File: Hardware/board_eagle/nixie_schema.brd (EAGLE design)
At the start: 150 x 170 mm, 110 parts, among them P1 100k, P2 10k, Q1 BC856B, Q3 BC856B, Q4 BCX70H, Q5 NTF5P03, U2 MC7940N

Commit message: Hopefully fixed compined tube footprint for good
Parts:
- moved N6 239.8 mm to (-5.00, -244.0), turned to 0 degrees
- moved N5 205.9 mm to (-5.00, -218.0), turned to 0 degrees
- moved N4 168.7 mm to (-5.00, -192.0), turned to 0 degrees
- moved N3 135.0 mm to (-5.00, -166.0), turned to 0 degrees
- moved N2 98.9 mm to (-5.00, -140.0), turned to 0 degrees
- moved N1 66.8 mm to (-5.00, -114.0), turned to 0 degrees
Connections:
- net N$10: now also N1.A(A); no longer N1.A(NC)
- net N$19: now also N2.A(A); no longer N2.A(NC)
- net N$2: now also N1.6(CAT); no longer N1.6(G)
- net N$21: now also N3.A(A); no longer N3.A(NC)
- net N$23: now also N2.6(CAT); no longer N2.6(G)
- net N$24: now also N1.9(DP); no longer N1.9(D)
- net N$25: now also N1.1(F); no longer N1.1(GRID)
- net N$26: now also N1.2(E); no longer N1.2(C)
- net N$27: now also N1.3(D); no longer N1.3(DP)
- net N$28: now also N1.4(CAT); no longer N1.4(B)
- net N$29: now also N1.5(NC); no longer N1.5(A)
- net N$31: now also N2.7(GRID); no longer N2.7(F)
- net N$32: now also N2.8(C); no longer N2.8(E)
- net N$33: now also N2.9(DP); no longer N2.9(D)
- net N$34: now also N2.0(B); no longer N2.0(CAT)
- net N$36: now also N3.6(CAT)
- net N$37: now also N3.7(GRID)
- net N$38: now also N2.5(NC); no longer N2.5(A)
- net N$39: now also N2.4(CAT); no longer N2.4(B)
- net N$40: now also N2.3(D); no longer N2.3(DP)
- net N$41: now also N2.2(E); no longer N2.2(C)
- net N$42: now also N2.1(F); no longer N2.1(GRID)
- net N$43: now also N3.8(C)
- net N$44: now also N3.9(DP)
- net N$45: now also N6.A(A); no longer N6.A(NC)
- net N$46: now also N3.0(B)
- net N$48: now also N4.6(CAT)
- net N$49: now also N3.5(NC)
- net N$50: now also N3.4(CAT)
- net N$51: now also N3.3(D)
- net N$52: now also N3.2(E)
- net N$53: now also N3.1(F)
- net N$54: now also N4.7(GRID)
- net N$55: now also N4.8(C)
- net N$56: now also N4.9(DP)
- net N$57: now also N4.0(B)
- net N$59: now also N4.5(NC)
- net N$6: now also N1.7(GRID); no longer N1.7(F)
- net N$60: now also N4.4(CAT)
- net N$61: now also N4.3(D)
- net N$62: now also N4.2(E)
- net N$63: now also N4.1(F)
- net N$64: now also N5.6(CAT)
- net N$65: now also N5.7(GRID)
- net N$66: now also N5.8(C)
- net N$67: now also N5.9(DP)
- net N$68: now also N5.0(B)
- net N$69: now also N5.5(NC)
- net N$7: now also N1.8(C); no longer N1.8(E)
- net N$70: now also N5.4(CAT)
- net N$71: now also N5.3(D)
- net N$72: now also N5.2(E)
- net N$73: now also N5.1(F)
- net N$76: now also N6.6(CAT)
- net N$77: now also N6.7(GRID)
- net N$78: now also N6.8(C)
- net N$79: now also N6.9(DP)
- net N$80: now also N6.5(NC)
- net N$81: now also N6.4(CAT)
- net N$82: now also N6.3(D)
- net N$83: now also N6.2(E)
- net N$84: now also N6.1(F)
- net N$86: now also N6.0(B)
- net N$88: now also N4.A(A); no longer N4.A(NC)
- net N$94: now also N1.0(B); no longer N1.0(CAT)
- net N$98: now also N5.A(A); no longer N5.A(NC)

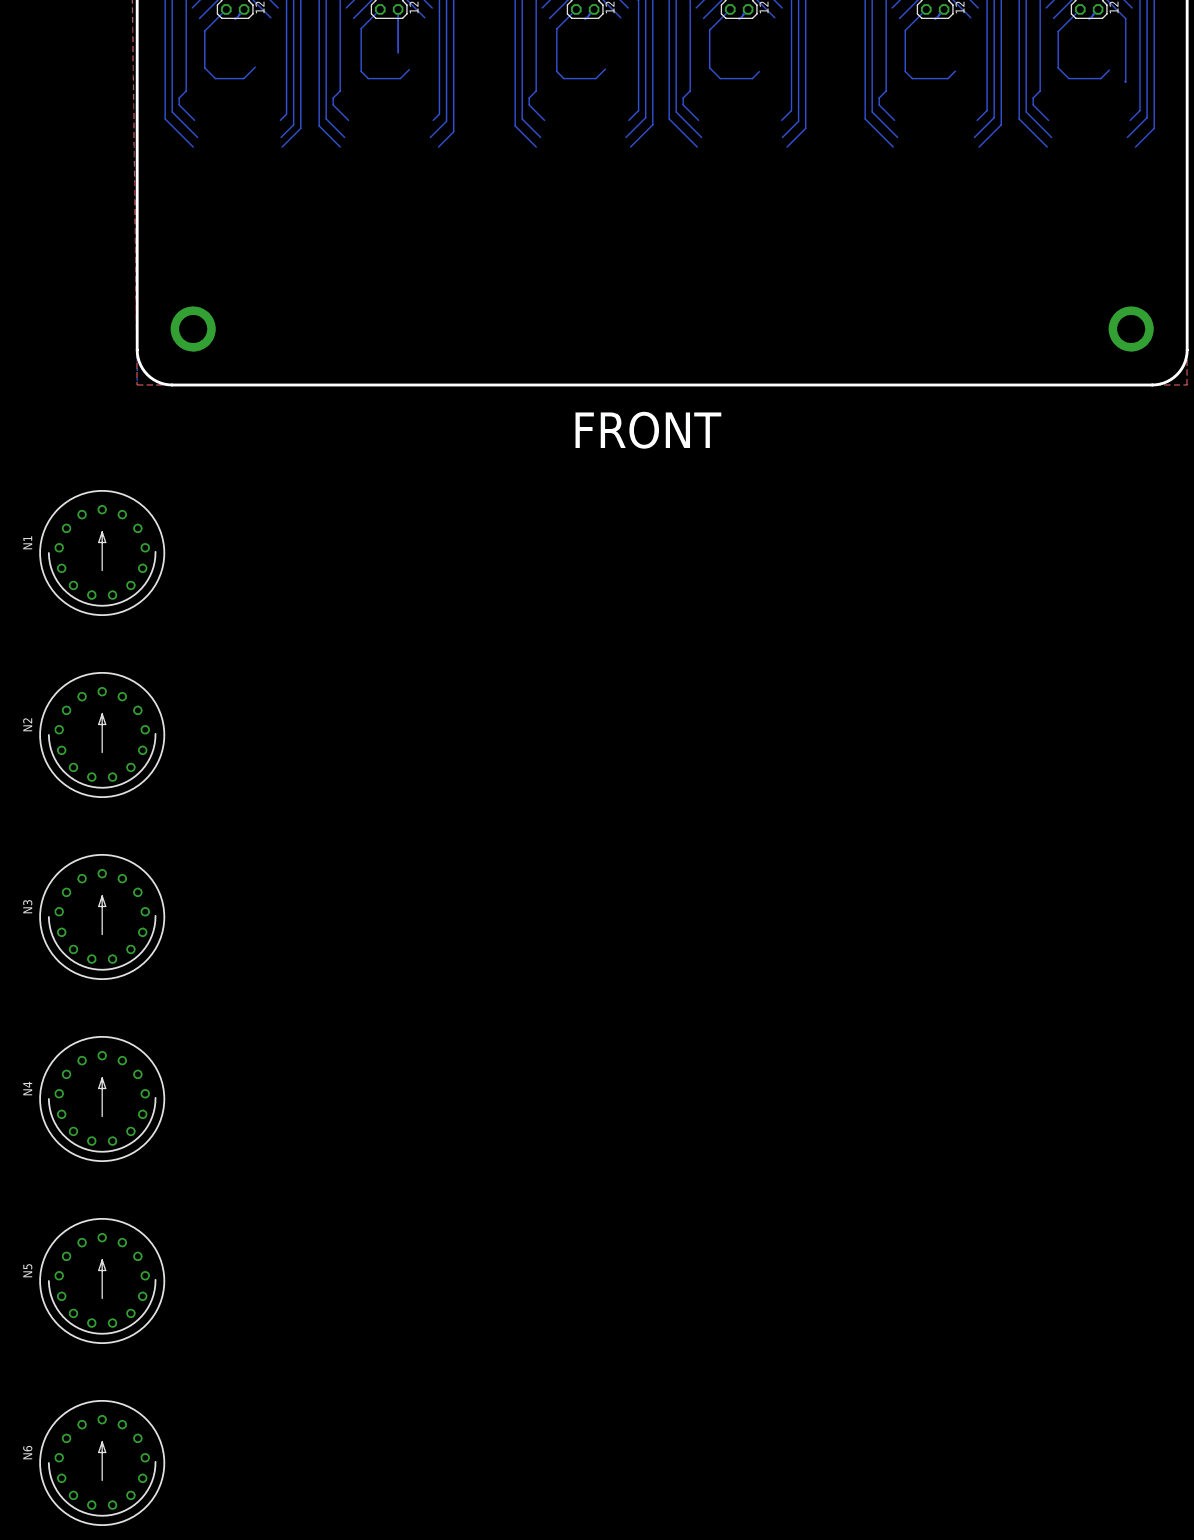
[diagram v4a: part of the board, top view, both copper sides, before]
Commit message: Added stuff for 1V5 rail for VFD cathodes
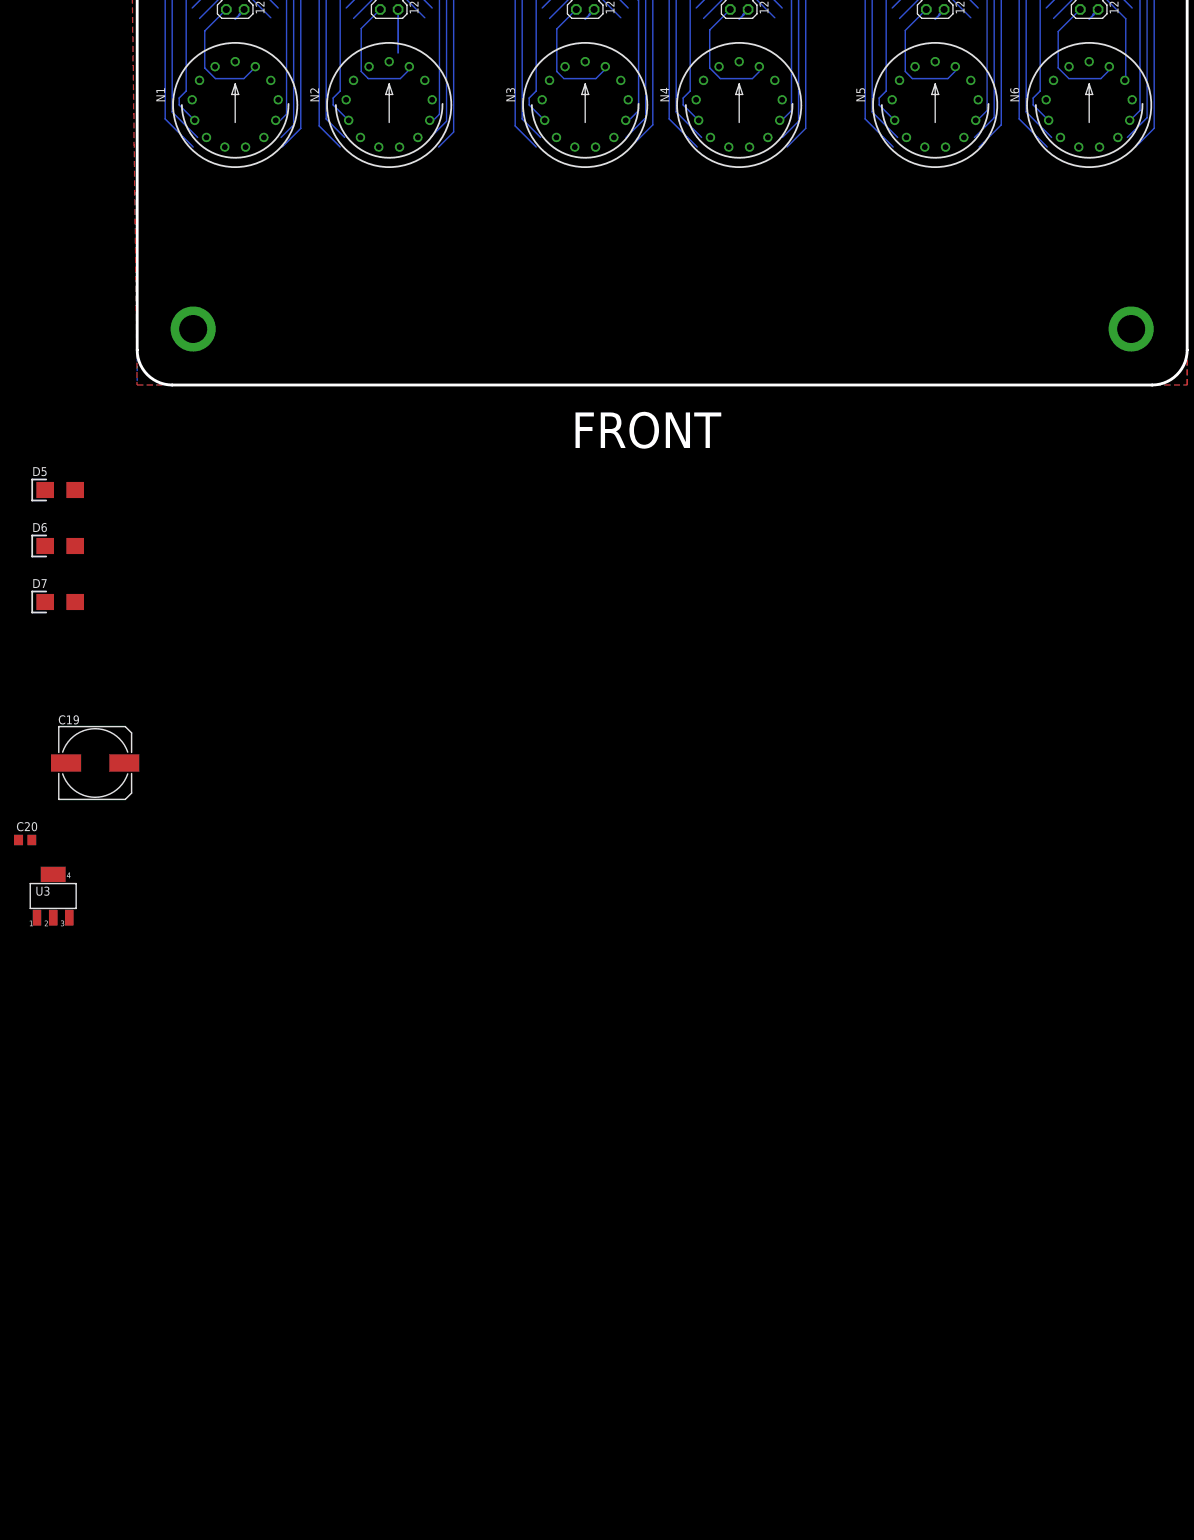
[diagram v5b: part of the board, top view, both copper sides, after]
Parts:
- added C19: 10u, rcl:153CLV-1014
- added C20: 100n, rcl:C0805
- added D5, D6, D7: B230A-13-F, nixe_cmp:SMA/SMB
- added U3: 1V5, nixe_cmp:SOT223
- moved N6 239.8 mm to (136.0, -50.0)
- moved N5 205.9 mm to (114.0, -50.0)
- moved N4 168.7 mm to (86.0, -50.0)
- moved N3 135.0 mm to (64.0, -50.0)
- moved N2 98.9 mm to (36.0, -50.0)
- moved N1 66.8 mm to (14.0, -50.0)
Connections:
- new net 1V5: C19.+, D7.C, U3.2, U3.4
- new net N$101: C20.1, D5.A, J7.2, U3.3
- new net N$104: D5.C, D6.A
- new net N$105: D6.C, D7.A
- net +3V3: no longer J7.2
- net GND: now also C19.-, C20.2, U3.1
- net VCC: no longer J7.1

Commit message: Figured out how to wire up tubes to support both IN-14 and IV-11
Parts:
- added BR1, BR12, BR2, BR6, BR7: HV_SOLDER_BRIDGE, nixe_cmp:HV_SOLDER_BRIDGE
- added CUT1, CUT11, CUT12, CUT5, CUT6, CUT7: CUT_TRACE, nixe_cmp:CUT_TRACE
- added R37, R38, R39, R40, R41, R42, R43, R44: 8.2k, rcl:R0603
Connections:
- removed net N$25: N1.1(F), SV7.9
- removed net N$27: N1.3(D), SV7.5
- removed net N$28: N1.4(CAT), SV7.3
- removed net N$6: N1.7(GRID), SV7.4
- removed net N$7: N1.8(C), SV7.6
- removed net N$94: N1.0(B), SV7.10
- new net 1_0_B: N1.0(B), R39.1, SV7.10
- new net 1_1_F: N1.1(F), R44.1, SV7.9
- new net 1_2_E: N1.2(E), R43.1, SV7.7
- new net 1_3_D: N1.3(D), R42.1, SV7.5
- new net 1_4_CAT: BR7.P$1, CUT11.P$2, N1.4(CAT)
- new net 1_5_NC: CUT12.P$2, N1.5(NC)
- new net 1_6_CAT: CUT6.P$1, N1.6(CAT)
- new net 1_7_GRID: BR1.P$1, CUT5.P$1, N1.7(GRID), R37.2, R38.2, R39.2, R40.2, R41.2, R42.2, R43.2, R44.2
- new net 1_8_C: N1.8(C), R41.1, SV7.6
- new net 1_9_DP: N1.9(DP), R40.1, SV7.8
- new net 1_A_A: BR6.P$1, CUT1.P$1, N1.A(A), R37.1
- new net 1_LDP_G: BR12.P$2, N1.LHDP(G), R38.1
- new net 1_RDP_NC: CUT7.P$2, N1.RHDP(NC)
- net GND: now also BR7.P$2
- net N$10: now also BR6.P$2, CUT6.P$2, SV7.2; no longer N1.A(A), SV7.12
- net N$2: now also BR1.P$2, CUT1.P$2, SV7.12; no longer N1.6(CAT), SV7.2
- net N$24: now also CUT5.P$2, SV7.4; no longer N1.9(DP), SV7.8
- net N$26: now also CUT7.P$1, SV7.11; no longer N1.2(E), SV7.7
- net N$29: now also BR12.P$1, CUT12.P$1; no longer N1.5(NC)
- net N$30: now also CUT11.P$1, SV7.3; no longer N1.RHDP(NC), SV7.11
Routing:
- net N$29: track 37.6 -> 0.00 mm
- net N$2: track 36.8 -> 0.00 mm
- net N$28: track 33.1 -> 0.00 mm
- net N$6: track 32.1 -> 0.00 mm
- net N$27: track 27.2 -> 0.00 mm
- net N$7: track 26.3 -> 0.00 mm
- net N$30: track 18.2 -> 0.00 mm
- net N$26: track 6.89 -> 0.00 mm
- net N$24: track 6.89 -> 0.00 mm
- net N$25: track 5.41 -> 0.00 mm
- net N$94: track 5.37 -> 0.00 mm
- net N$10: track 1.93 -> 0.00 mm

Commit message: Finished tube schematic layout
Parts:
- added BR10, BR11, BR13, BR14, BR15, BR16, BR17, BR18, BR19, BR20, BR21, BR22, BR23, BR24, BR25, BR26, BR27, BR28, BR29, BR3, BR30, BR4, BR5, BR8, BR9: HV_SOLDER_BRIDGE, nixe_cmp:HV_SOLDER_BRIDGE
- added CUT10, CUT13, CUT14, CUT15, CUT16, CUT17, CUT18, CUT19, CUT2, CUT20, CUT21, CUT22, CUT23, CUT24, CUT25, CUT26, CUT27, CUT28, CUT29, CUT3, CUT30, CUT31, CUT32, CUT33, CUT34, CUT35, CUT36, CUT4, CUT8, CUT9: CUT_TRACE, nixe_cmp:CUT_TRACE
- added R45, R46, R47, R48, R49, R50, R51, R52, R53, R54, R55, R56, R57, R58, R59, R60, R61, R62, R63, R64, R65, R66, R67, R68, R69, R70, R71, R72, R73, R74, R75, R76, R77, R78, R79, R80, R81, R82, R83, R84: 8.2k, rcl:R0603
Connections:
- removed net N$52: N3.2(E), SV9.7
- removed net N$53: N3.1(F), SV9.9
- removed net N$54: N4.7(GRID), SV10.4
- removed net N$55: N4.8(C), SV10.6
- removed net N$56: N4.9(DP), SV10.8
- removed net N$57: N4.0(B), SV10.10
- removed net N$58: N5.RHDP(NC), SV11.11
- removed net N$59: N4.5(NC), SV10.1
- removed net N$60: N4.4(CAT), SV10.3
- removed net N$61: N4.3(D), SV10.5
- removed net N$62: N4.2(E), SV10.7
- removed net N$63: N4.1(F), SV10.9
- removed net N$64: N5.6(CAT), SV11.2
- removed net N$65: N5.7(GRID), SV11.4
- removed net N$66: N5.8(C), SV11.6
- removed net N$67: N5.9(DP), SV11.8
- removed net N$68: N5.0(B), SV11.10
- removed net N$69: N5.5(NC), SV11.1
- removed net N$70: N5.4(CAT), SV11.3
- removed net N$71: N5.3(D), SV11.5
- removed net N$72: N5.2(E), SV11.7
- removed net N$73: N5.1(F), SV11.9
- removed net N$75: N6.RHDP(NC), SV12.11
- removed net N$76: N6.6(CAT), SV12.2
- removed net N$77: N6.7(GRID), SV12.4
- removed net N$78: N6.8(C), SV12.6
- removed net N$79: N6.9(DP), SV12.8
- removed net N$80: N6.5(NC), SV12.1
- removed net N$81: N6.4(CAT), SV12.3
- removed net N$82: N6.3(D), SV12.5
- removed net N$83: N6.2(E), SV12.7
- removed net N$84: N6.1(F), SV12.9
- removed net N$86: N6.0(B), SV12.10
- removed net N$88: N4.A(A), SV10.12
- removed net N$98: N5.A(A), SV11.12
- new net 2_0_B: N2.0(B), R47.1, SV8.10
- new net 2_1_F: N2.1(F), R52.1, SV8.9
- new net 2_2_E: N2.2(E), R51.1, SV8.7
- new net 2_3_D: N2.3(D), R50.1, SV8.5
- new net 2_4_CAT: BR3.P$1, CUT9.P$2, N2.4(CAT)
- new net 2_5_NC: CUT10.P$2, N2.5(NC)
- new net 2_6_CAT: BR4.P$2, CUT4.P$1, N2.6(CAT)
- new net 2_7_GRID: BR5.P$1, CUT3.P$1, N2.7(GRID), R45.2, R46.2, R47.2, R48.2, R49.2, R50.2, R51.2, R52.2
- new net 2_8_C: N2.8(C), R49.1, SV8.6
- new net 2_9_DP: N2.9(DP), R48.1, SV8.8
- new net 2_A_A: BR8.P$1, CUT2.P$1, N2.A(A), R45.1
- new net 2_LDP_G: BR9.P$2, N2.LHDP(G), R46.1
- new net 2_RDP_NC: CUT8.P$2, N2.RHDP(NC)
- new net 3_0_B: N3.0(B), R55.1, SV9.10
- new net 3_1_F: N3.1(F), R60.1, SV9.9
- new net 3_2_E: N3.2(E), R59.1, SV9.7
- new net 3_3_D: N3.3(D), R58.1, SV9.5
- new net 3_4_CAT: BR10.P$1, CUT17.P$2, N3.4(CAT)
- new net 3_5_NC: CUT18.P$2, N3.5(NC)
- new net 3_6_CAT: BR11.P$2, CUT15.P$1, N3.6(CAT)
- new net 3_7_GRID: BR13.P$1, CUT14.P$1, N3.7(GRID), R53.2, R54.2, R55.2, R56.2, R57.2, R58.2, R59.2, R60.2
- new net 3_8_C: N3.8(C), R57.1, SV9.6
- new net 3_9_DP: N3.9(DP), R56.1, SV9.8
- new net 3_A_A: BR14.P$1, CUT13.P$1, N3.A(A), R53.1
- new net 3_LDP_G: BR15.P$2, N3.LHDP(G), R54.1
- new net 3_RDP_NC: CUT16.P$2, N3.RHDP(NC)
- new net 4_0_B: N4.0(B), R63.1, SV10.10
- new net 4_1_F: N4.1(F), R68.1, SV10.9
- new net 4_2_E: N4.2(E), R67.1, SV10.7
- new net 4_3_D: N4.3(D), R66.1, SV10.5
- new net 4_4_CAT: BR19.P$1, CUT23.P$2, N4.4(CAT)
- new net 4_5_NC: CUT24.P$2, N4.5(NC)
- new net 4_6_CAT: BR20.P$2, CUT21.P$1, N4.6(CAT)
- new net 4_7_GRID: BR16.P$1, CUT20.P$1, N4.7(GRID), R61.2, R62.2, R63.2, R64.2, R65.2, R66.2, R67.2, R68.2
- new net 4_8_C: N4.8(C), R65.1, SV10.6
- new net 4_9_DP: N4.9(DP), R64.1, SV10.8
- new net 4_A_A: BR17.P$1, CUT19.P$1, N4.A(A), R61.1
- new net 4_LDP_G: BR18.P$2, N4.LHDP(G), R62.1
- new net 4_RDP_NC: CUT22.P$2, N4.RHDP(NC)
- new net 5_0_B: N5.0(B), R71.1, SV11.10
- new net 5_1_F: N5.1(F), R76.1, SV11.9
- new net 5_2_E: N5.2(E), R75.1, SV11.7
- new net 5_3_D: N5.3(D), R74.1, SV11.5
- new net 5_4_CAT: BR21.P$1, CUT29.P$2, N5.4(CAT)
- new net 5_5_NC: CUT30.P$2, N5.5(NC)
- new net 5_6_CAT: BR22.P$2, CUT27.P$1, N5.6(CAT)
- new net 5_7_GRID: BR23.P$1, CUT26.P$1, N5.7(GRID), R69.2, R70.2, R71.2, R72.2, R73.2, R74.2, R75.2, R76.2
- new net 5_8_C: N5.8(C), R73.1, SV11.6
- new net 5_9_DP: N5.9(DP), R72.1, SV11.8
- new net 5_A_A: BR24.P$1, CUT25.P$1, N5.A(A), R69.1
- new net 5_LDP_G: BR25.P$2, N5.LHDP(G), R70.1
- new net 5_RDP_NC: CUT28.P$2, N5.RHDP(NC)
- new net 6_0_B: N6.0(B), R79.1, SV12.10
- new net 6_1_F: N6.1(F), R84.1, SV12.9
- new net 6_2_E: N6.2(E), R83.1, SV12.7
- new net 6_3_D: N6.3(D), R82.1, SV12.5
- new net 6_4_CAT: BR26.P$1, CUT35.P$2, N6.4(CAT)
- new net 6_5_NC: CUT36.P$2, N6.5(NC)
- new net 6_6_CAT: BR27.P$2, CUT33.P$1, N6.6(CAT)
- new net 6_7_GRID: BR28.P$1, CUT32.P$1, N6.7(GRID), R77.2, R78.2, R79.2, R80.2, R81.2, R82.2, R83.2, R84.2
- new net 6_8_C: N6.8(C), R81.1, SV12.6
- new net 6_9_DP: N6.9(DP), R80.1, SV12.8
- new net 6_A_A: BR29.P$1, CUT31.P$1, N6.A(A), R77.1
- new net 6_LDP_G: BR30.P$2, N6.LHDP(G), R78.1
- new net 6_RDP_NC: CUT34.P$2, N6.RHDP(NC)
- new net N$25: CUT9.P$1, SV8.3
- new net N$27: BR14.P$2, CUT15.P$2, SV9.2
- new net N$28: CUT14.P$2, SV9.4
- new net N$6: BR8.P$2, CUT4.P$2, SV8.2
- new net N$7: CUT3.P$2, SV8.4
- net 1V5: now also BR11.P$1, BR2.P$1, BR20.P$1, BR22.P$1, BR27.P$1, BR4.P$1
- net 1_6_CAT: now also BR2.P$2
- net GND: now also BR10.P$2, BR19.P$2, BR21.P$2, BR26.P$2, BR3.P$2
- net N$1: now also BR5.P$2, CUT2.P$2, SV8.12; no longer N2.RHDP(NC), SV8.11
- net N$19: now also CUT8.P$1, SV8.11; no longer N2.A(A), SV8.12
- net N$21: now also BR13.P$2, CUT13.P$2; no longer N3.A(A)
- net N$23: now also BR9.P$1, CUT10.P$1, SV8.1; no longer N2.6(CAT), SV8.2
- net N$31: now also CUT16.P$1, SV9.11; no longer N2.7(GRID), SV8.4
- net N$32: now also BR15.P$1, CUT18.P$1, SV9.1; no longer N2.8(C), SV8.6
- net N$33: now also CUT17.P$1, SV9.3; no longer N2.9(DP), SV8.8
- net N$34: now also BR16.P$2, CUT19.P$2, SV10.12; no longer N2.0(B), SV8.10
- net N$35: now also BR17.P$2, CUT21.P$2, SV10.2; no longer N3.RHDP(NC), SV9.11
- net N$36: now also CUT20.P$2, SV10.4; no longer N3.6(CAT), SV9.2
- net N$37: now also CUT22.P$1, SV10.11; no longer N3.7(GRID), SV9.4
- net N$38: now also BR18.P$1, CUT24.P$1, SV10.1; no longer N2.5(NC), SV8.1
- net N$39: now also CUT23.P$1, SV10.3; no longer N2.4(CAT), SV8.3
- net N$40: now also BR23.P$2, CUT25.P$2, SV11.12; no longer N2.3(D), SV8.5
- net N$41: now also BR24.P$2, CUT27.P$2, SV11.2; no longer N2.2(E), SV8.7
- net N$42: now also CUT26.P$2, SV11.4; no longer N2.1(F), SV8.9
- net N$43: now also CUT28.P$1, SV11.11; no longer N3.8(C), SV9.6
- net N$44: now also BR25.P$1, CUT30.P$1, SV11.1; no longer N3.9(DP), SV9.8
- net N$45: now also BR28.P$2, CUT31.P$2; no longer N6.A(A)
- net N$46: now also CUT29.P$1, SV11.3; no longer N3.0(B), SV9.10
- net N$47: now also BR29.P$2, CUT33.P$2, SV12.2; no longer N4.RHDP(NC), SV10.11
- net N$48: now also CUT32.P$2, SV12.4; no longer N4.6(CAT), SV10.2
- net N$49: now also CUT34.P$1, SV12.11; no longer N3.5(NC), SV9.1
- net N$50: now also BR30.P$1, CUT36.P$1, SV12.1; no longer N3.4(CAT), SV9.3
- net N$51: now also CUT35.P$1, SV12.3; no longer N3.3(D), SV9.5
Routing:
- net N$69: track 37.6 -> 0.00 mm
- net N$59: track 37.6 -> 0.00 mm
- net N$80: track 37.6 -> 0.00 mm
- net N$49: track 37.2 -> 0.00 mm
- net N$38: track 37.2 -> 0.00 mm
- net N$36: track 37.2 -> 0.00 mm
- net N$64: track 37.1 -> 0.00 mm
- net N$48: track 36.9 -> 0.00 mm
- net N$76: track 36.8 -> 0.00 mm
- net N$23: track 36.5 -> 0.00 mm
- net N$70: track 33.1 -> 0.00 mm
- net N$60: track 33.1 -> 0.00 mm
- net N$81: track 33.1 -> 0.00 mm
- net N$50: track 32.7 -> 0.00 mm
- net N$39: track 32.7 -> 0.00 mm
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
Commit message: Some initial experimental routing for the top board
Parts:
- D5, D6, D7: value B230A-13-F -> (none)
- moved CUT32 417.3 mm to (164.0, -144.0), flipped to the bottom
- moved CUT34 417.3 mm to (164.0, -148.0), flipped to the bottom
- moved CUT36 417.3 mm to (164.0, -152.0), flipped to the bottom
- moved R77 416.4 mm to (163.0, -108.0), flipped to the bottom
- moved R79 416.4 mm to (163.0, -113.0), flipped to the bottom
- moved R81 416.4 mm to (163.0, -118.0), flipped to the bottom
- moved R83 416.4 mm to (163.0, -123.0), flipped to the bottom
- moved BR26 415.6 mm to (162.0, -128.0), flipped to the bottom
- moved BR28 415.6 mm to (162.0, -132.0), flipped to the bottom
- moved BR29 415.6 mm to (162.0, -136.0), flipped to the bottom
- moved BR30 415.6 mm to (162.0, -140.0), flipped to the bottom
- moved CUT33 411.4 mm to (157.0, -144.0), flipped to the bottom
- moved CUT35 411.4 mm to (157.0, -148.0), flipped to the bottom
- moved R78 411.4 mm to (157.0, -108.0), flipped to the bottom
- moved R80 411.4 mm to (157.0, -113.0), flipped to the bottom
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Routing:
- net N$2: track 0.00 -> 53.3 mm, vias 0 -> 3
- net N$101: track 0.00 -> 51.9 mm
- net N$26: track 0.00 -> 42.3 mm, vias 0 -> 3
- net 1_7_GRID: track 0.00 -> 38.0 mm
- net 1V5: track 0.00 -> 34.8 mm
- net 2_3_D: track 0.00 -> 26.5 mm
- net 3_8_C: track 0.00 -> 26.5 mm
- net 6_8_C: track 0.00 -> 26.4 mm
- net 6_3_D: track 0.00 -> 26.4 mm
- net 3_3_D: track 0.00 -> 26.4 mm
- net 4_3_D: track 0.00 -> 26.4 mm
- net 2_8_C: track 0.00 -> 26.4 mm
- net 1_8_C: track 0.00 -> 26.4 mm
- net 1_3_D: track 0.00 -> 26.4 mm
- net 5_8_C: track 0.00 -> 26.4 mm
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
